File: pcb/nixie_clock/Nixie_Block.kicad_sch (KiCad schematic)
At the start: 25 parts, among them U66 MSD42WT1G, U67 MSD42WT1G, U68 MSD42WT1G, U69 MSD42WT1G, U70 MSD42WT1G, U71 MSD42WT1G, U72 MSD42WT1G, U73 MSD42WT1G, U74 MSD42WT1G, U75 MSD42WT1G, U76 MSD42WT1G, U77 MSD42WT1G

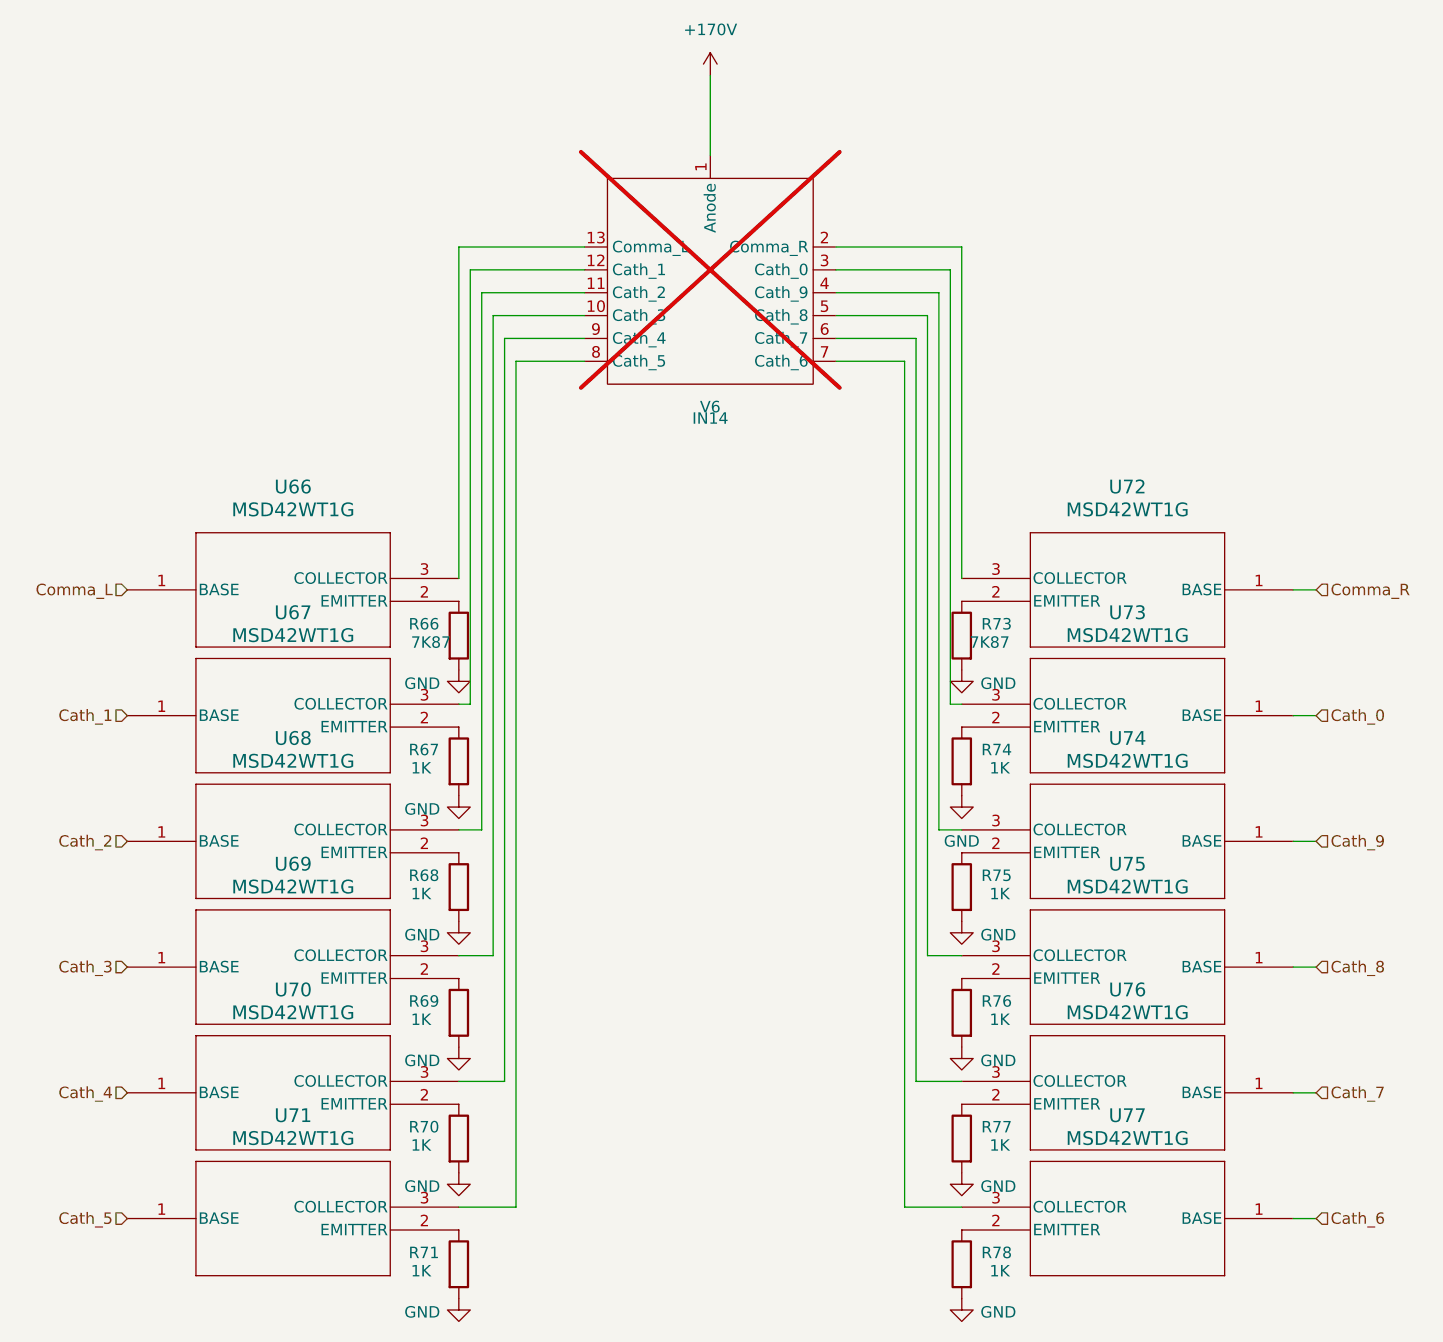
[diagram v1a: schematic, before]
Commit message: updated to kicad9
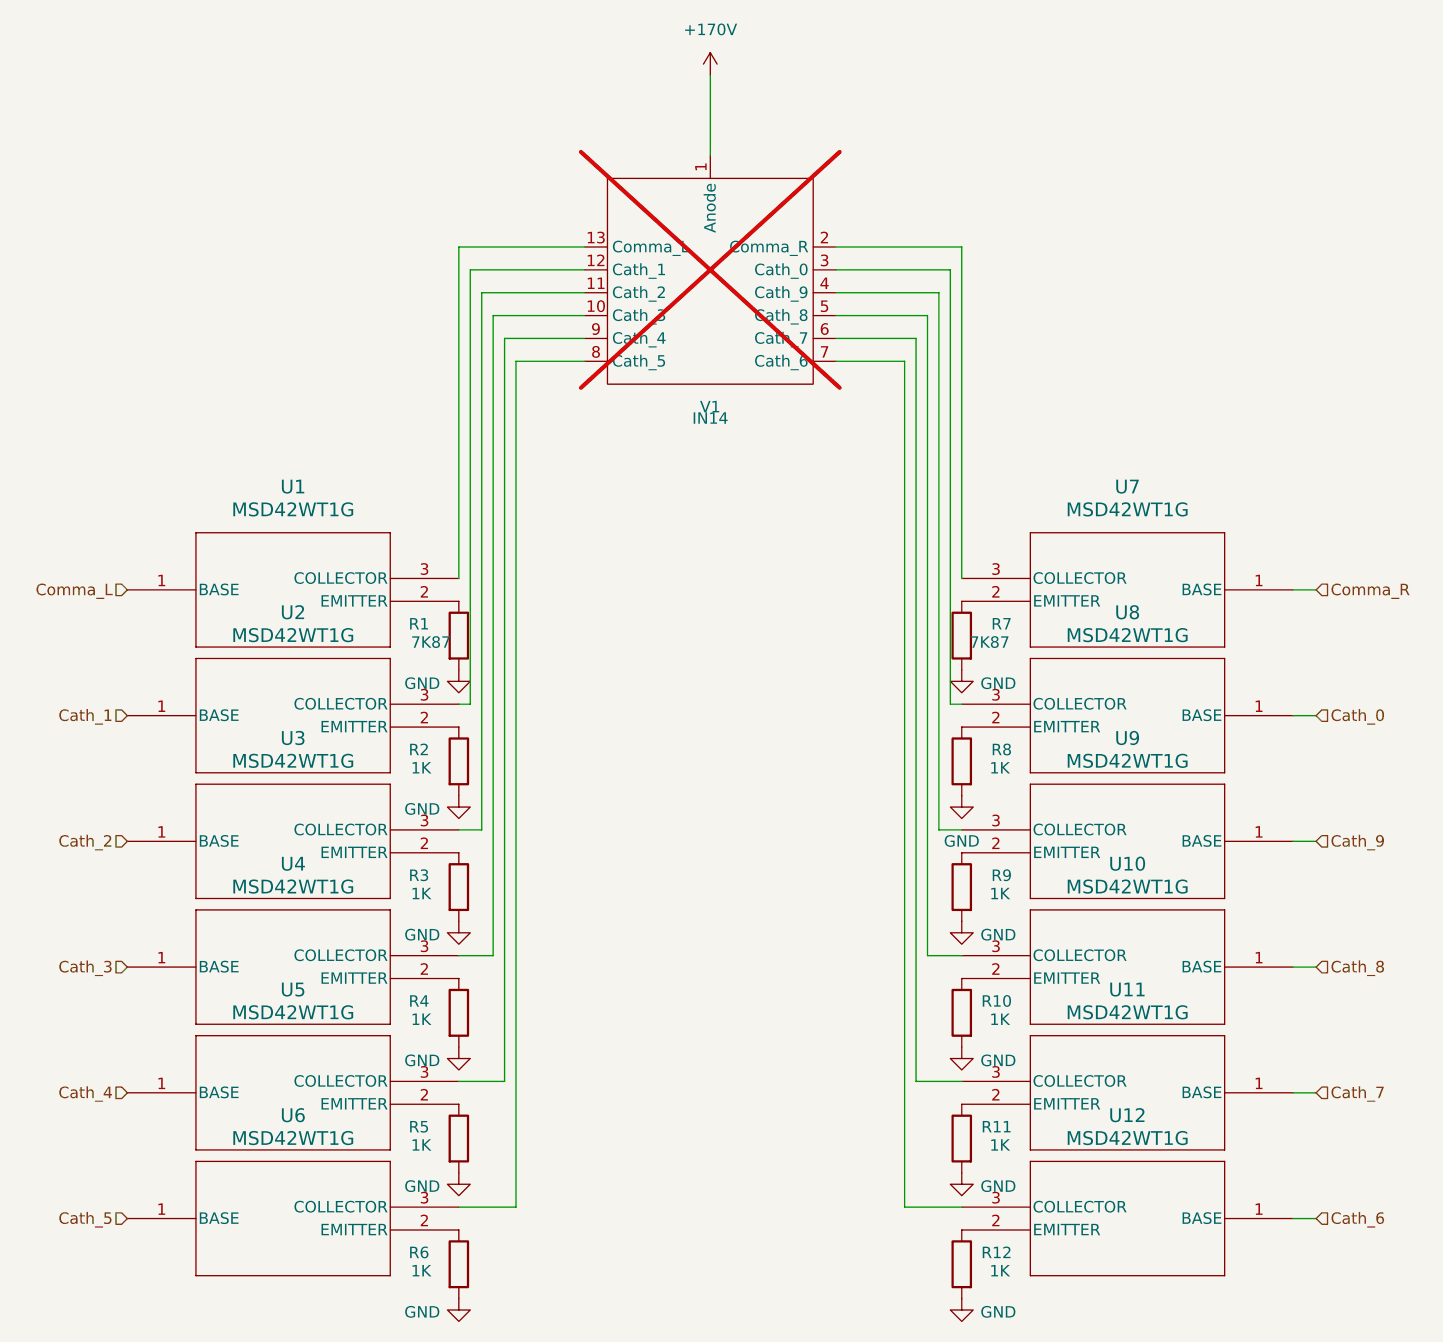
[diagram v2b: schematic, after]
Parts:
- renumbered R66 to R1, R76 to R10, R77 to R11, R78 to R12, R67 to R2, R68 to R3, R69 to R4, R70 to R5, R71 to R6, R73 to R7, R74 to R8, R75 to R9, U66 to U1, U75 to U10, U76 to U11, U77 to U12, U67 to U2, U68 to U3, U69 to U4, U70 to U5, U71 to U6, U72 to U7, U73 to U8, U74 to U9, V6 to V1
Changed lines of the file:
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@@
 (kicad_sch
-	(version 20231120)
+	(version 20250114)
 	(generator "eeschema")
-	(generator_version "8.0")
+	(generator_version "9.0")
 	(paper "A4")
 	(wire
@@
 		(shape input)
 		(at 36.83 105.41 180)
-		(fields_autoplaced yes)
 		(effects
 			(font
@@
 		(shape input)
 		(at 168.91 119.38 0)
-		(fields_autoplaced yes)
 		(effects
 			(font
@@
 		(shape input)
 		(at 168.91 91.44 0)
-		(fields_autoplaced yes)
 		(effects
 			(font
@@
 		(shape input)
 		(at 36.83 91.44 180)
-		(fields_autoplaced yes)
 		(effects
 			(font
@@
 		(shape input)
 		(at 168.91 133.35 0)
-		(fields_autoplaced yes)
 		(effects
 			(font
@@
 		(shape input)
 		(at 36.83 119.38 180)
-		(fields_autoplaced yes)
 		(effects
 			(font
@@
 		(shape input)
 		(at 168.91 147.32 0)
-		(fields_autoplaced yes)
 		(effects
 			(font
@@
 		(shape input)
 		(at 168.91 105.41 0)
-		(fields_autoplaced yes)
 		(effects
 			(font
@@
 		(shape input)
 		(at 36.83 161.29 180)
-		(fields_autoplaced yes)
 		(effects
 			(font
@@
 		(shape input)
 		(at 36.83 147.32 180)
-		(fields_autoplaced yes)
 		(effects
 			(font
@@
 		(shape input)
 		(at 36.83 133.35 180)
-		(fields_autoplaced yes)
 		(effects
 			(font
@@
 		(shape input)
 		(at 168.91 161.29 0)
-		(fields_autoplaced yes)
 		(effects
 			(font
@@
 		(on_board yes)
 		(dnp no)
-		(property "Reference" "#PWR077"
+		(property "Reference" "#PWR03"
 			(at 73.66 120.65 0)
 			(effects
@@
 		(on_board yes)
 		(dnp no)
-		(property "Reference" "R69"
+		(property "Reference" "R4"
 			(at 68.072 137.16 0)
 			(effects
@@
 		(on_board yes)
 		(dnp no)
-		(property "Reference" "R75"
+		(property "Reference" "R9"
 			(at 135.128 123.19 0)
 			(effects
@@
 		(dnp no)
 		(fields_autoplaced yes)
-		(property "Reference" "U69"
+		(property "Reference" "U4"
 			(at 55.245 121.92 0)
 			(effects
@@
 		(dnp no)
 		(fields_autoplaced yes)
-		(property "Reference" "U70"
+		(property "Reference" "U5"
 			(at 55.245 135.89 0)
 			(effects
@@
 		(on_board yes)
 		(dnp no)
-		(property "Reference" "R78"
+		(property "Reference" "R12"
 			(at 135.128 165.1 0)
 			(effects
@@
 		(dnp no)
 		(fields_autoplaced yes)
-		(property "Reference" "U71"
+		(property "Reference" "U6"
 			(at 55.245 149.86 0)
 			(effects
@@
 		(on_board yes)
 		(dnp no)
-		(property "Reference" "#PWR078"
+		(property "Reference" "#PWR04"
 			(at 73.66 134.62 0)
 			(effects
@@
 		(on_board yes)
 		(dnp no)
-		(property "Reference" "#PWR087"
+		(property "Reference" "#PWR013"
 			(at 129.54 162.56 0)
 			(effects
@@
 		(dnp no)
 		(fields_autoplaced yes)
-		(property "Reference" "U77"
+		(property "Reference" "U12"
 			(at 147.955 149.86 0)
 			(effects
@@
 		(on_board yes)
 		(dnp no)
-		(property "Reference" "#PWR085"
+		(property "Reference" "#PWR011"
 			(at 129.54 134.62 0)
 			(effects
@@
 		(dnp no)
 		(fields_autoplaced yes)
-		(property "Reference" "U76"
+		(property "Reference" "U11"
 			(at 147.955 135.89 0)
 			(effects
@@
 		(dnp no)
 		(fields_autoplaced yes)
-		(property "Reference" "#PWR082"
+		(property "Reference" "#PWR08"
 			(at 101.6 38.1 0)
 			(effects
@@
 		(on_board yes)
 		(dnp no)
-		(property "Reference" "R66"
+		(property "Reference" "R1"
 			(at 68.072 95.25 0)
 			(effects
@@
 		(on_board yes)
 		(dnp no)
-		(property "Reference" "R73"
+		(property "Reference" "R7"
 			(at 135.128 95.25 0)
 			(effects
@@
 		(on_board yes)
 		(dnp no)
-		(property "Reference" "R74"
+		(property "Reference" "R8"
 			(at 135.128 109.22 0)
 			(effects
@@
 		(on_board yes)
 		(dnp no)
-		(property "Reference" "#PWR081"
+		(property "Reference" "#PWR07"
 			(at 73.66 176.53 0)
 			(effects
@@
 		(on_board yes)
 		(dnp no)
-		(property "Reference" "#PWR080"
+		(property "Reference" "#PWR06"
 			(at 73.66 162.56 0)
 			(effects
@@
 		(on_board yes)
 		(dnp no)
-		(property "Reference" "#PWR076"
+		(property "Reference" "#PWR02"
 			(at 73.66 106.68 0)
 			(effects
@@
 		(dnp no)
 		(fields_autoplaced yes)
-		(property "Reference" "U66"
+		(property "Reference" "U1"
 			(at 55.245 80.01 0)
 			(effects
@@
 		(on_board yes)
 		(dnp no)
-		(property "Reference" "R70"
+		(property "Reference" "R5"
 			(at 68.072 151.13 0)
 			(effects
@@
 		(dnp no)
 		(fields_autoplaced yes)
-		(property "Reference" "U75"
+		(property "Reference" "U10"
 			(at 147.955 121.92 0)
 			(effects
@@
 		(on_board yes)
 		(dnp no)
-		(property "Reference" "R77"
+		(property "Reference" "R11"
 			(at 135.128 151.13 0)
 			(effects
@@
 		(dnp no)
 		(fields_autoplaced yes)
-		(property "Reference" "U74"
+		(property "Reference" "U9"
 			(at 147.955 107.95 0)
 			(effects
@@
 		(on_board yes)
 		(dnp no)
-		(property "Reference" "#PWR079"
+		(property "Reference" "#PWR05"
 			(at 73.66 148.59 0)
 			(effects
@@
 		(on_board yes)
 		(dnp no)
-		(property "Reference" "#PWR088"
+		(property "Reference" "#PWR019"
 			(at 129.54 176.53 0)
 			(effects
@@
 		(on_board yes)
 		(dnp no)
-		(property "Reference" "#PWR083"
+		(property "Reference" "#PWR09"
 			(at 129.54 106.68 0)
 			(effects
@@
 		(on_board yes)
 		(dnp yes)
-		(property "Reference" "V6"
+		(property "Reference" "V1"
 			(at 101.6 71.12 0)
 			(effects
@@
 		(dnp no)
 		(fields_autoplaced yes)
-		(property "Reference" "U67"
+		(property "Reference" "U2"
 			(at 55.245 93.98 0)
 			(effects
@@
 		(on_board yes)
 		(dnp no)
-		(property "Reference" "R68"
+		(property "Reference" "R3"
 			(at 68.072 123.19 0)
 			(effects
@@
 		(dnp no)
 		(fields_autoplaced yes)
-		(property "Reference" "U72"
+		(property "Reference" "U7"
 			(at 147.955 80.01 0)
 			(effects
@@
 		(dnp no)
 		(fields_autoplaced yes)
-		(property "Reference" "U68"
+		(property "Reference" "U3"
 			(at 55.245 107.95 0)
 			(effects
@@
 		(dnp no)
 		(fields_autoplaced yes)
-		(property "Reference" "#PWR084"
+		(property "Reference" "#PWR010"
 			(at 129.54 120.65 0)
 			(effects
@@
 		(on_board yes)
 		(dnp no)
-		(property "Reference" "R76"
+		(property "Reference" "R10"
 			(at 135.128 137.16 0)
 			(effects
@@
 		(on_board yes)
 		(dnp no)
-		(property "Reference" "#PWR086"
+		(property "Reference" "#PWR012"
 			(at 129.54 148.59 0)
 			(effects
@@
 		(on_board yes)
 		(dnp no)
-		(property "Reference" "R67"
+		(property "Reference" "R2"
 			(at 68.072 109.22 0)
 			(effects
@@
 		(on_board yes)
 		(dnp no)
-		(property "Reference" "R71"
+		(property "Reference" "R6"
 			(at 68.072 165.1 0)
 			(effects
@@
 		(dnp no)
 		(fields_autoplaced yes)
-		(property "Reference" "U73"
+		(property "Reference" "U8"
 			(at 147.955 93.98 0)
 			(effects
@@
 		)
 	)
+	(embedded_fonts no)
 )
